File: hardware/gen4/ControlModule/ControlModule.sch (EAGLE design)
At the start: 22 parts, among them IC1 XMEGA16A4A

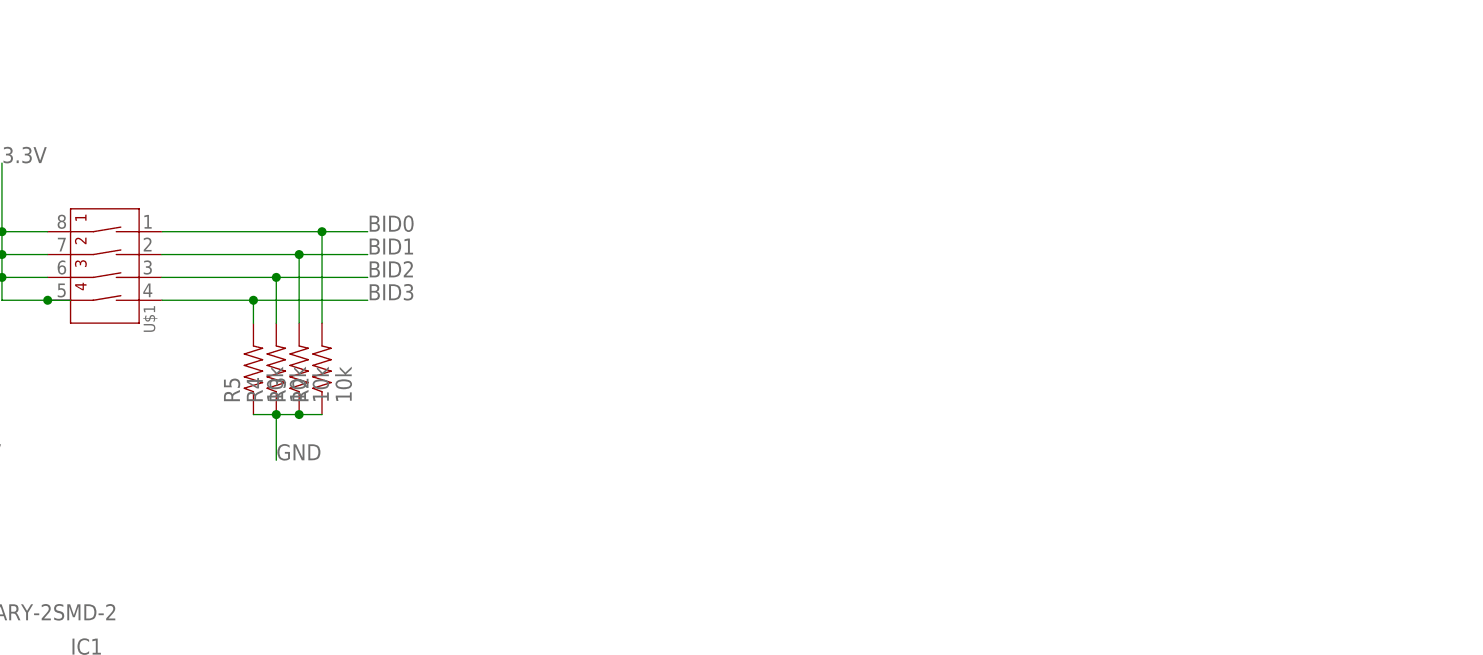
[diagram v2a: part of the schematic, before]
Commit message: Added 3.3V regulator
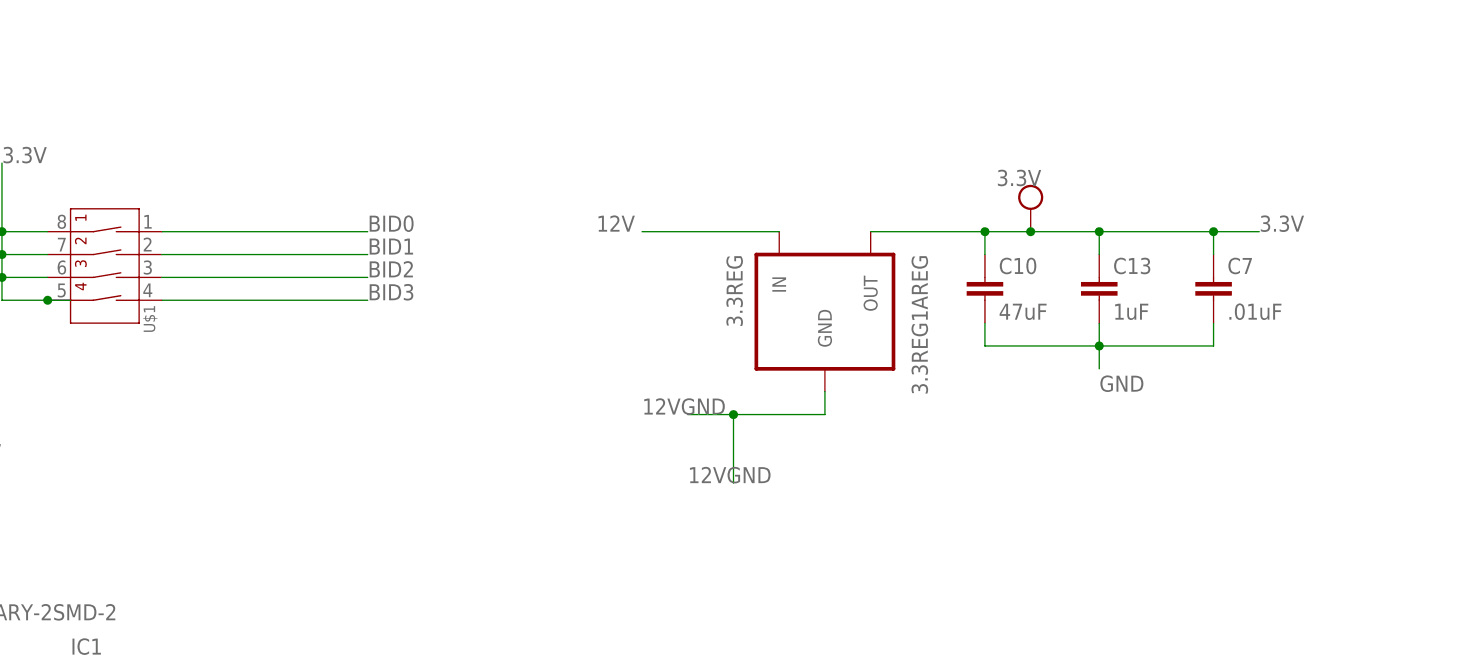
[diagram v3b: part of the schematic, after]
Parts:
- removed R2, R3, R4, R5: 10k, SparkFun-Resistors:RESISTOR0805-RES
- added 3.3REG: 3.3REG1AREG, gen3:3.3REG1AREG
- added 3.3V: TEST_PT, gen3:TEST_PT
- added C10: 47uF, SparkFun-Capacitors:CAP1206
- added C13: 1uF, SparkFun-Capacitors:CAP0805
- added C7: .01uF, SparkFun-Capacitors:CAP0805
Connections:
- new net 12VGND: 3.3REG.GND
- net 12V: now also 3.3REG.IN
- net 3.3V: now also 3.3REG.OUT, 3.3V.P$1, C10.1, C13.1, C7.1
- net BID0: no longer R2.2
- net BID1: no longer R3.2
- net BID2: no longer R4.2
- net BID3: no longer R5.2
- net GND: now also C10.2, C13.2, C7.2; no longer R2.1, R3.1, R4.1, R5.1
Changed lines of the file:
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@@
 <part name="C3" library="SparkFun-Capacitors" deviceset="CAP" device="0805" value="0.1uF"/>
 <part name="U$1" library="SparkFun-Electromechanical" deviceset="4-POS-DIP" device=""/>
-<part name="R2" library="SparkFun-Resistors" deviceset="RESISTOR" device="0805-RES" value="10k"/>
-<part name="R3" library="SparkFun-Resistors" deviceset="RESISTOR" device="0805-RES" value="10k"/>
-<part name="R4" library="SparkFun-Resistors" deviceset="RESISTOR" device="0805-RES" value="10k"/>
-<part name="R5" library="SparkFun-Resistors" deviceset="RESISTOR" device="0805-RES" value="10k"/>
 <part name="XBEE" library="SparkFun-RF" deviceset="XBEE-1" device="B1"/>
 <part name="C11" library="SparkFun-Capacitors" deviceset="CAP" device="0805" value=".01uF"/>
@@
 <part name="R8" library="SparkFun-Passives" deviceset="RESISTOR" device="0805-RES" value="80k"/>
 <part name="R9" library="SparkFun-Passives" deviceset="RESISTOR" device="0805-RES" value="20k"/>
+<part name="C13" library="SparkFun-Capacitors" deviceset="CAP" device="0805" value="1uF"/>
+<part name="3.3V" library="gen3" deviceset="TEST_PT" device=""/>
+<part name="3.3REG" library="gen3" deviceset="3.3REG1A" device="REG"/>
+<part name="C7" library="SparkFun-Capacitors" deviceset="CAP" device="0805" value=".01uF"/>
+<part name="C10" library="SparkFun-Capacitors" deviceset="CAP" device="1206" value="47uF"/>
 </parts>
 <sheets>
@@
 <instance part="C3" gate="G$1" x="25.4" y="76.2" rot="R90"/>
 <instance part="U$1" gate="G$1" x="53.34" y="144.78" rot="R270"/>
-<instance part="R2" gate="G$1" x="81.28" y="127" rot="R90"/>
-<instance part="R3" gate="G$1" x="78.74" y="127" rot="R90"/>
-<instance part="R4" gate="G$1" x="76.2" y="127" rot="R90"/>
-<instance part="R5" gate="G$1" x="73.66" y="127" rot="R90"/>
 <instance part="XBEE" gate="G$1" x="200.66" y="60.96"/>
 <instance part="C11" gate="G$1" x="172.72" y="76.2"/>
@@
 <instance part="R8" gate="G$1" x="127" y="83.82" rot="R90"/>
 <instance part="R9" gate="G$1" x="127" y="68.58" rot="R90"/>
+<instance part="C13" gate="G$1" x="167.64" y="134.62"/>
+<instance part="3.3V" gate="G$1" x="160.02" y="144.78"/>
+<instance part="3.3REG" gate="G$1" x="137.16" y="134.62" rot="MR270"/>
+<instance part="C7" gate="G$1" x="180.34" y="134.62"/>
+<instance part="C10" gate="G$1" x="154.94" y="134.62"/>
 </instances>
 <busses>
@@
 </segment>
 <segment>
-<pinref part="R5" gate="G$1" pin="1"/>
-<pinref part="R4" gate="G$1" pin="1"/>
-<wire x1="73.66" y1="121.92" x2="76.2" y2="121.92" width="0.1524" layer="91"/>
-<pinref part="R3" gate="G$1" pin="1"/>
-<wire x1="78.74" y1="121.92" x2="76.2" y2="121.92" width="0.1524" layer="91"/>
-<junction x="76.2" y="121.92"/>
-<pinref part="R2" gate="G$1" pin="1"/>
-<wire x1="81.28" y1="121.92" x2="78.74" y2="121.92" width="0.1524" layer="91"/>
-<junction x="78.74" y="121.92"/>
-<wire x1="76.2" y1="121.92" x2="76.2" y2="116.84" width="0.1524" layer="91"/>
-<label x="76.2" y="116.84" size="1.778" layer="95"/>
-</segment>
-<segment>
 <pinref part="XBEE" gate="G$1" pin="GND"/>
 <wire x1="180.34" y1="48.26" x2="175.26" y2="48.26" width="0.1524" layer="91"/>
@@
 <wire x1="127" y1="63.5" x2="127" y2="60.96" width="0.1524" layer="91"/>
 <label x="127" y="60.96" size="1.778" layer="95"/>
+</segment>
+<segment>
+<wire x1="154.94" y1="132.08" x2="154.94" y2="129.54" width="0.1524" layer="91"/>
+<label x="167.64" y="124.46" size="1.778" layer="95"/>
+<pinref part="C13" gate="G$1" pin="2"/>
+<wire x1="167.64" y1="132.08" x2="167.64" y2="129.54" width="0.1524" layer="91"/>
+<wire x1="167.64" y1="129.54" x2="154.94" y2="129.54" width="0.1524" layer="91"/>
+<pinref part="C7" gate="G$1" pin="2"/>
+<wire x1="180.34" y1="132.08" x2="180.34" y2="129.54" width="0.1524" layer="91"/>
+<wire x1="167.64" y1="129.54" x2="180.34" y2="129.54" width="0.1524" layer="91"/>
+<junction x="167.64" y="129.54"/>
+<wire x1="167.64" y1="129.54" x2="167.64" y2="127" width="0.1524" layer="91"/>
+<pinref part="C10" gate="G$1" pin="2"/>
 </segment>
 </net>
@@
 <label x="40.64" y="116.84" size="1.778" layer="95"/>
 </segment>
+<segment>
+<wire x1="167.64" y1="142.24" x2="180.34" y2="142.24" width="0.1524" layer="91"/>
+<wire x1="180.34" y1="142.24" x2="185.42" y2="142.24" width="0.1524" layer="91"/>
+<label x="185.42" y="142.24" size="1.778" layer="95"/>
+<pinref part="C13" gate="G$1" pin="1"/>
+<wire x1="167.64" y1="139.7" x2="167.64" y2="142.24" width="0.1524" layer="91"/>
+<pinref part="C7" gate="G$1" pin="1"/>
+<wire x1="180.34" y1="142.24" x2="180.34" y2="139.7" width="0.1524" layer="91"/>
+<junction x="180.34" y="142.24"/>
+<pinref part="3.3V" gate="G$1" pin="P$1"/>
+<wire x1="167.64" y1="142.24" x2="160.02" y2="142.24" width="0.1524" layer="91"/>
+<junction x="167.64" y="142.24"/>
+<wire x1="154.94" y1="139.7" x2="154.94" y2="142.24" width="0.1524" layer="91"/>
+<wire x1="160.02" y1="142.24" x2="154.94" y2="142.24" width="0.1524" layer="91"/>
+<junction x="160.02" y="142.24"/>
+<pinref part="3.3REG" gate="G$1" pin="OUT"/>
+<wire x1="142.24" y1="142.24" x2="154.94" y2="142.24" width="0.1524" layer="91"/>
+<junction x="154.94" y="142.24"/>
+<pinref part="C10" gate="G$1" pin="1"/>
+</segment>
 </net>
 <net name="N$1" class="0">
@@
 <segment>
 <pinref part="U$1" gate="G$1" pin="1A"/>
-<wire x1="63.5" y1="142.24" x2="81.28" y2="142.24" width="0.1524" layer="91"/>
+<wire x1="63.5" y1="142.24" x2="86.36" y2="142.24" width="0.1524" layer="91"/>
 <label x="86.36" y="142.24" size="1.778" layer="95"/>
-<pinref part="R2" gate="G$1" pin="2"/>
-<wire x1="81.28" y1="142.24" x2="86.36" y2="142.24" width="0.1524" layer="91"/>
-<wire x1="81.28" y1="132.08" x2="81.28" y2="142.24" width="0.1524" layer="91"/>
-<junction x="81.28" y="142.24"/>
 </segment>
 </net>
@@
 <segment>
 <pinref part="U$1" gate="G$1" pin="3A"/>
-<wire x1="63.5" y1="137.16" x2="76.2" y2="137.16" width="0.1524" layer="91"/>
+<wire x1="63.5" y1="137.16" x2="86.36" y2="137.16" width="0.1524" layer="91"/>
 <label x="86.36" y="137.16" size="1.778" layer="95"/>
-<pinref part="R4" gate="G$1" pin="2"/>
-<wire x1="76.2" y1="137.16" x2="86.36" y2="137.16" width="0.1524" layer="91"/>
-<wire x1="76.2" y1="132.08" x2="76.2" y2="137.16" width="0.1524" layer="91"/>
-<junction x="76.2" y="137.16"/>
 </segment>
 </net>
@@
 <segment>
 <pinref part="U$1" gate="G$1" pin="2A"/>
-<wire x1="63.5" y1="139.7" x2="78.74" y2="139.7" width="0.1524" layer="91"/>
+<wire x1="63.5" y1="139.7" x2="86.36" y2="139.7" width="0.1524" layer="91"/>
 <label x="86.36" y="139.7" size="1.778" layer="95"/>
-<pinref part="R3" gate="G$1" pin="2"/>
-<wire x1="78.74" y1="139.7" x2="86.36" y2="139.7" width="0.1524" layer="91"/>
-<wire x1="78.74" y1="132.08" x2="78.74" y2="139.7" width="0.1524" layer="91"/>
-<junction x="78.74" y="139.7"/>
 </segment>
 </net>
@@
 <segment>
 <pinref part="U$1" gate="G$1" pin="4A"/>
-<wire x1="63.5" y1="134.62" x2="73.66" y2="134.62" width="0.1524" layer="91"/>
 <label x="86.36" y="134.62" size="1.778" layer="95"/>
-<pinref part="R5" gate="G$1" pin="2"/>
-<wire x1="73.66" y1="134.62" x2="86.36" y2="134.62" width="0.1524" layer="91"/>
-<wire x1="73.66" y1="132.08" x2="73.66" y2="134.62" width="0.1524" layer="91"/>
-<junction x="73.66" y="134.62"/>
+<wire x1="63.5" y1="134.62" x2="86.36" y2="134.62" width="0.1524" layer="91"/>
 </segment>
 </net>
@@
 <label x="127" y="91.44" size="1.778" layer="95"/>
 </segment>
+<segment>
+<pinref part="3.3REG" gate="G$1" pin="IN"/>
+<wire x1="116.84" y1="142.24" x2="132.08" y2="142.24" width="0.1524" layer="91"/>
+<label x="111.76" y="142.24" size="1.778" layer="95"/>
+</segment>
 </net>
 <net name="SS_1" class="0">
@@
 </segment>
 </net>
+<net name="12VGND" class="0">
+<segment>
+<pinref part="3.3REG" gate="G$1" pin="GND"/>
+<wire x1="121.92" y1="121.92" x2="127" y2="121.92" width="0.1524" layer="91"/>
+<wire x1="127" y1="121.92" x2="137.16" y2="121.92" width="0.1524" layer="91"/>
+<wire x1="137.16" y1="121.92" x2="137.16" y2="124.46" width="0.1524" layer="91"/>
+<label x="116.84" y="121.92" size="1.778" layer="95"/>
+<wire x1="127" y1="121.92" x2="127" y2="114.3" width="0.1524" layer="91"/>
+<junction x="127" y="121.92"/>
+<label x="121.92" y="114.3" size="1.778" layer="95"/>
+</segment>
+</net>

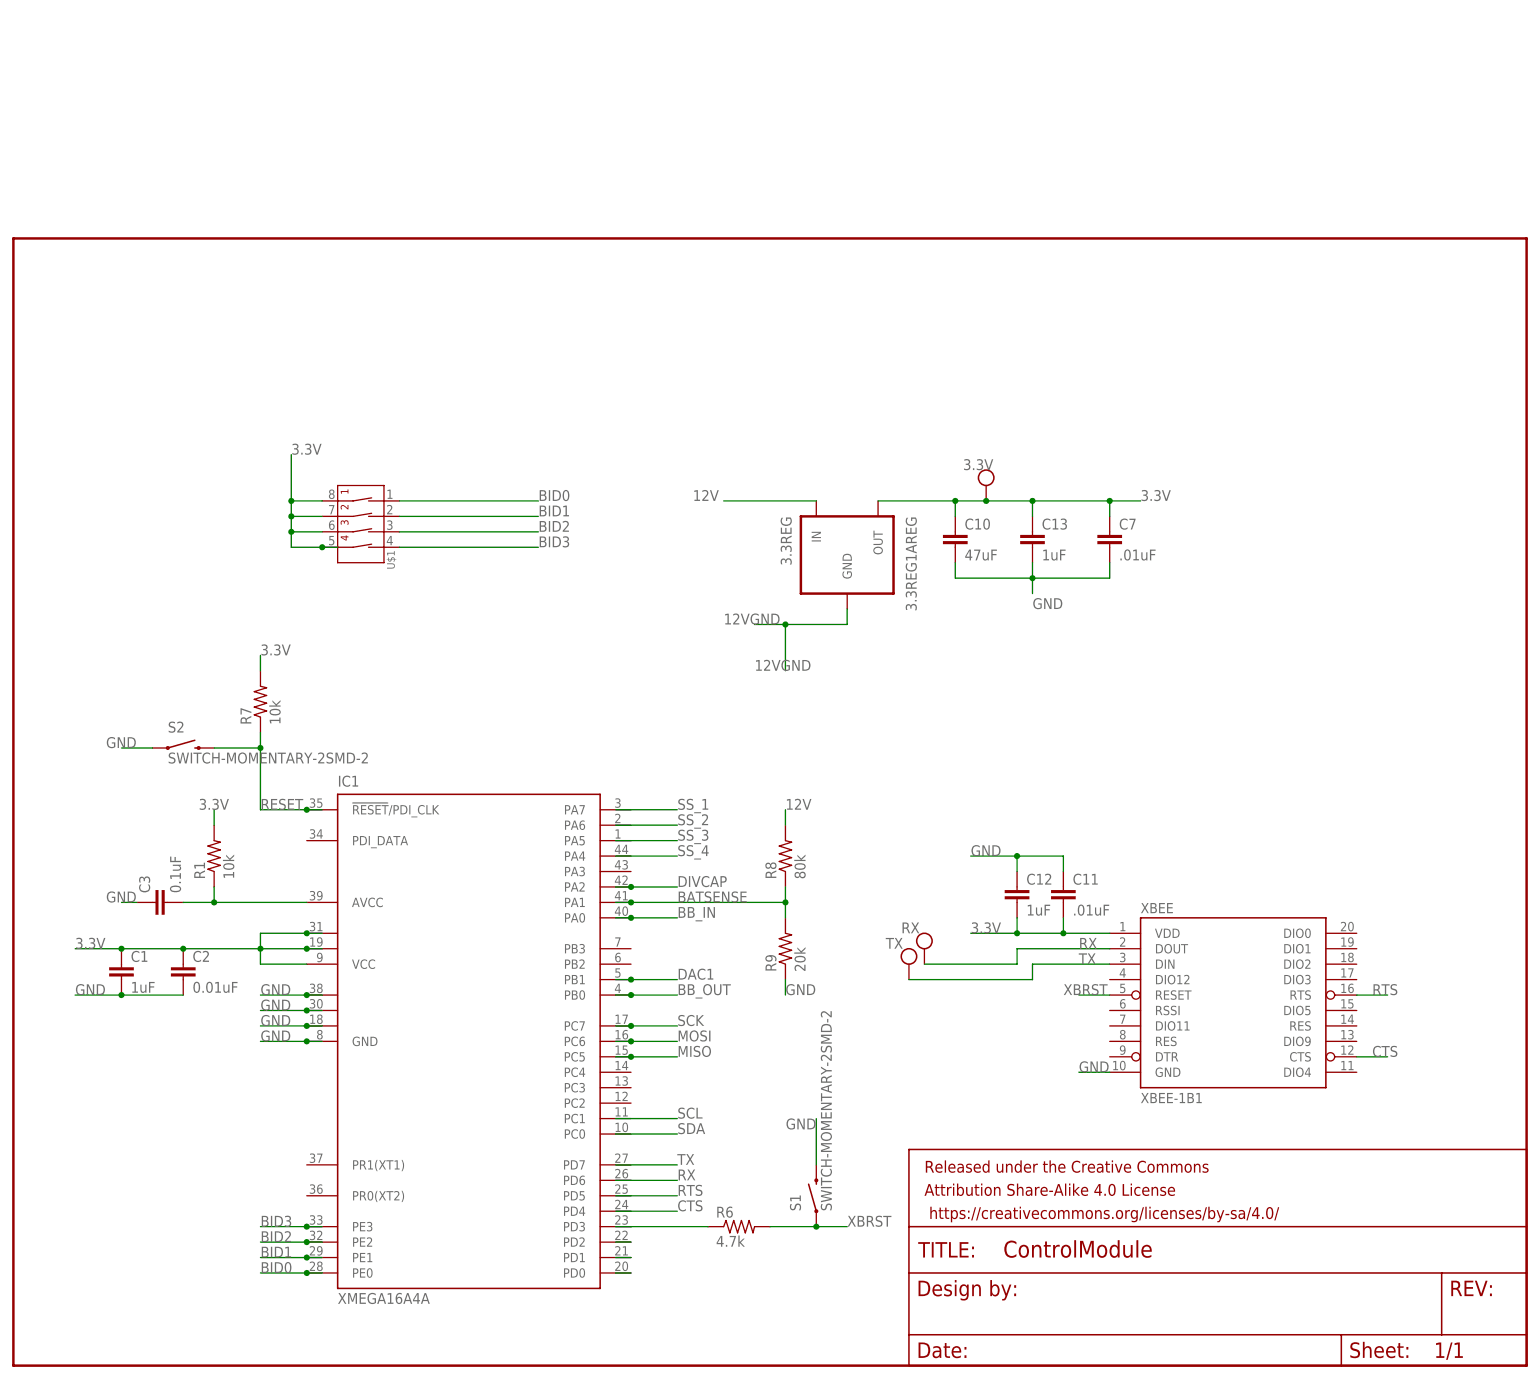
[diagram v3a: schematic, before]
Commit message: Added headers, IMU, LEDs
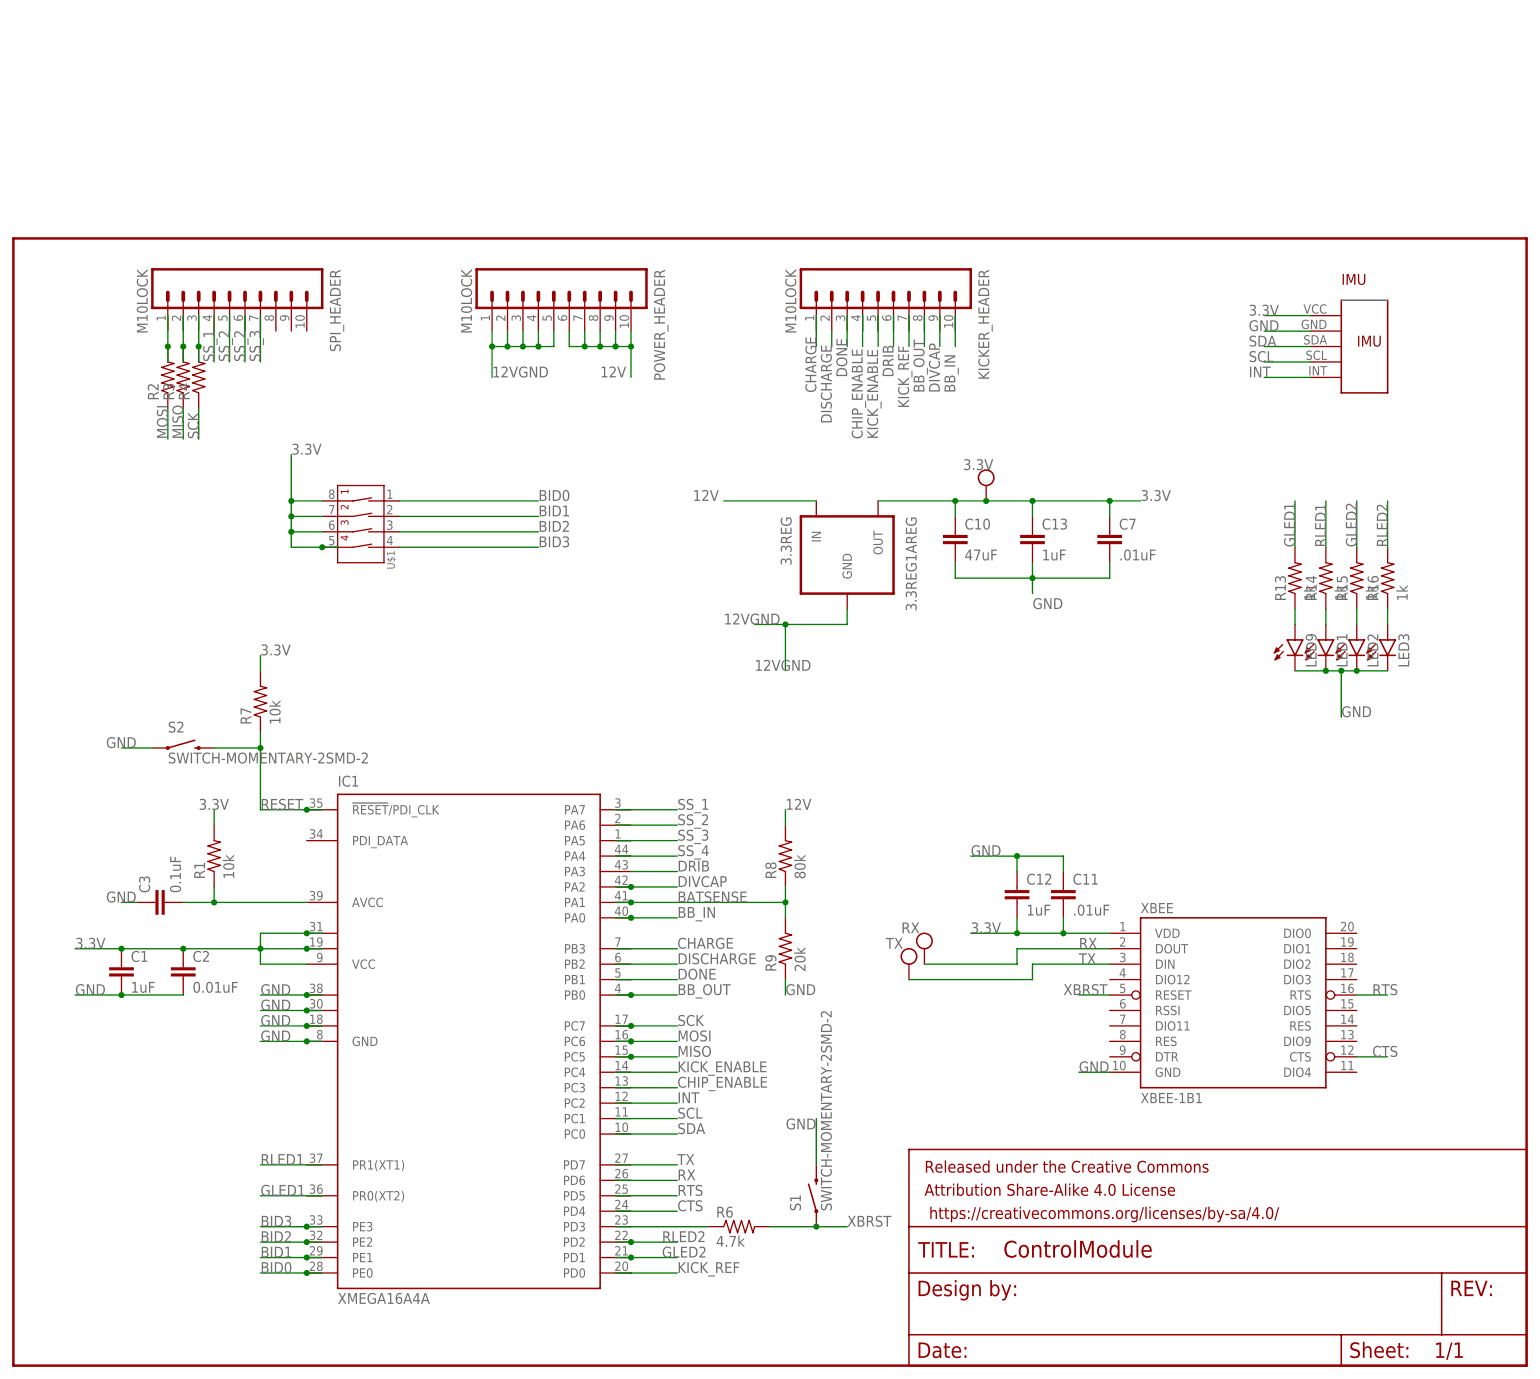
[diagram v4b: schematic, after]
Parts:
- added IMU: MPU6050IMUMPU, gen3:MPU6050IMUMPU
- added KICKER_HEADER, POWER_HEADER, SPI_HEADER: M10LOCK, SparkFun-Connectors:M10LOCK
- added LED1, LED2, LED3, LED9: (no value), SparkFun-LED:LED1206
- added R13, R14, R15, R16: 1k, SparkFun-Passives:RESISTOR0805-RES
- added R2, R3, R4: (no value), SparkFun-Resistors:RESISTOR0805-RES
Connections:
- net DAC1 renamed DONE
- net N$2 renamed KICK_REF
- removed net N$3: IC1.PD1
- removed net N$4: IC1.PD2
- new net DISCHARGE: KICKER_HEADER.2
- new net DRIB: IC1.PA3
- new net GLED1: R13.2
- new net GLED2: IC1.PD1, R15.2
- new net INT: IMU.INT
- new net N$10: LED2.A, R15.1
- new net N$11: LED3.A, R16.1
- new net N$2: LED9.A, R13.1
- new net N$6: R2.2
- new net N$7: R3.2
- new net N$8: R4.2
- new net N$9: LED1.A, R14.1
- new net RLED1: R14.2
- new net RLED2: IC1.PD2, R16.2
- new net SCL: IMU.SCL
- new net SDA: IMU.SDA
- net 12V: now also POWER_HEADER.10, POWER_HEADER.6, POWER_HEADER.7, POWER_HEADER.8, POWER_HEADER.9
- net 12VGND: now also POWER_HEADER.1, POWER_HEADER.2, POWER_HEADER.3, POWER_HEADER.4, POWER_HEADER.5
- net 3.3V: now also IMU.VCC
- net GND: now also IMU.GND, LED1.C, LED2.C, LED3.C, LED9.C
- net MISO: now also R3.1
- net MOSI: now also R2.1
- net SCK: now also R4.1
